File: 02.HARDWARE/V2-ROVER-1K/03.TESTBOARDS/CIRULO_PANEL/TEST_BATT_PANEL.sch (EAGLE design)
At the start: 14 parts, among them J1 302-S201, Q1 PJA3416AE_R1_00001, U3 ATE1D-5M3-10-Z

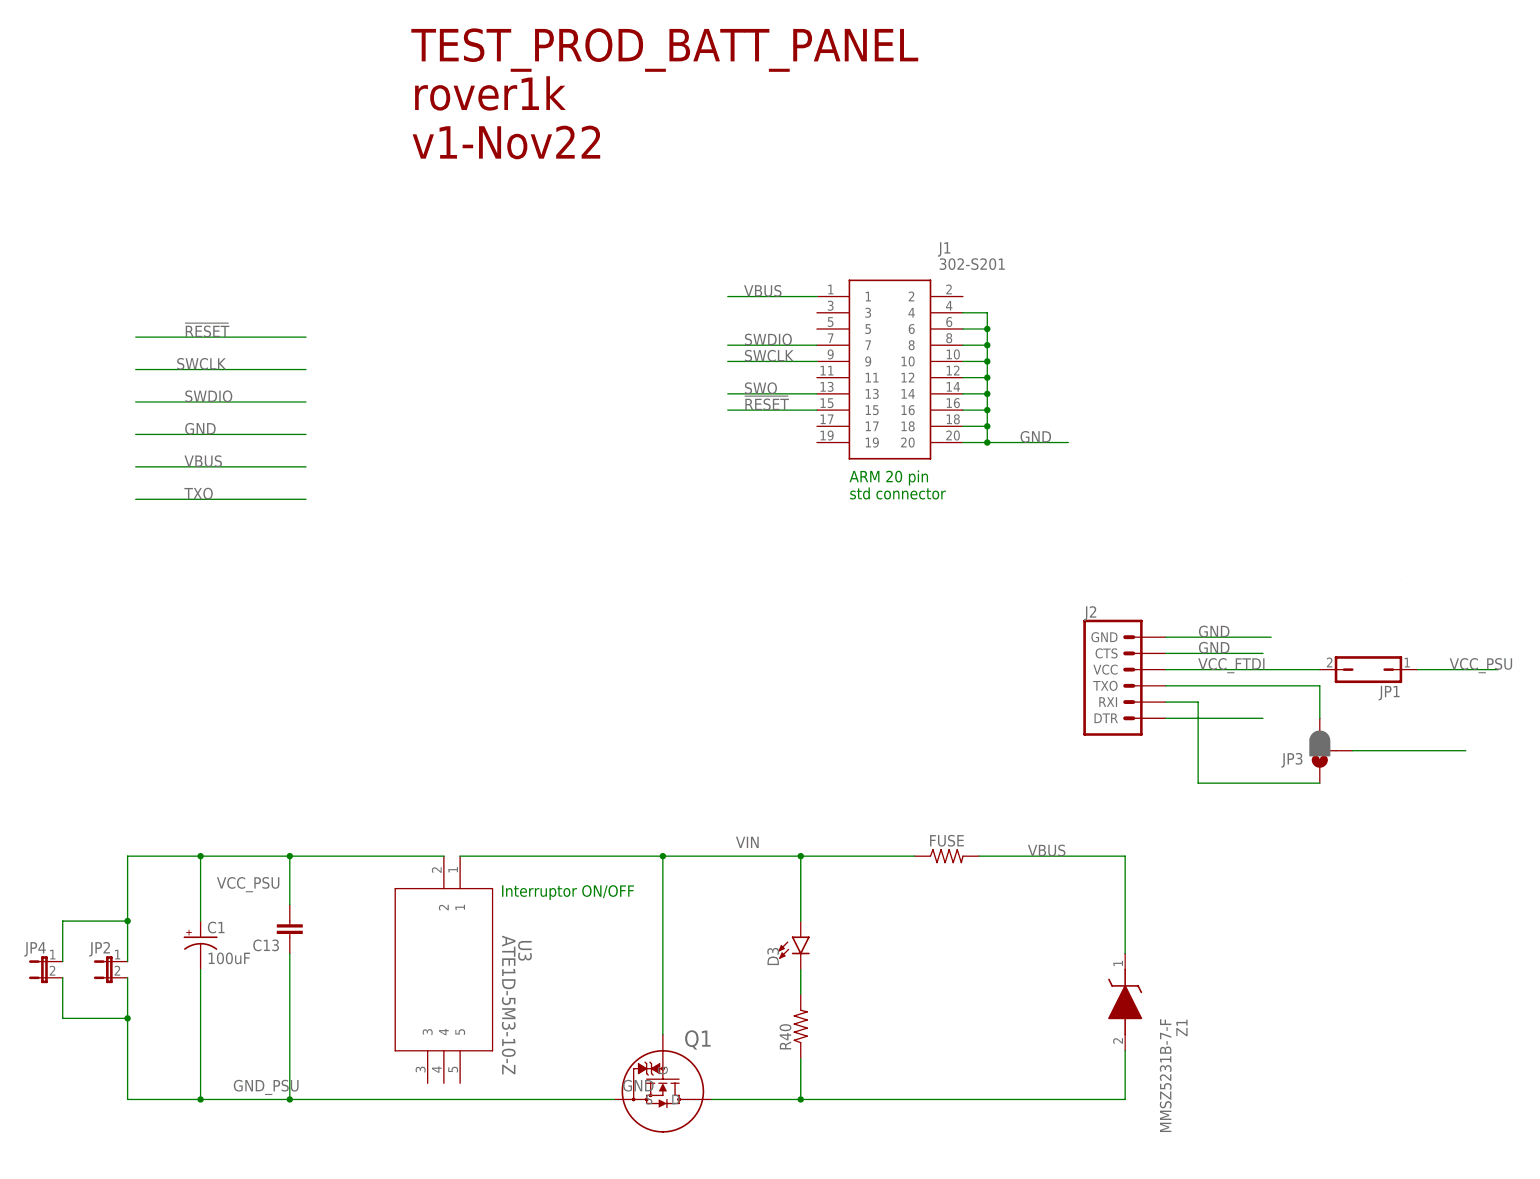
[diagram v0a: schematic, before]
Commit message: Versiones v2 pendientes de revision de conjunto de PCBs Cirulo programacion.
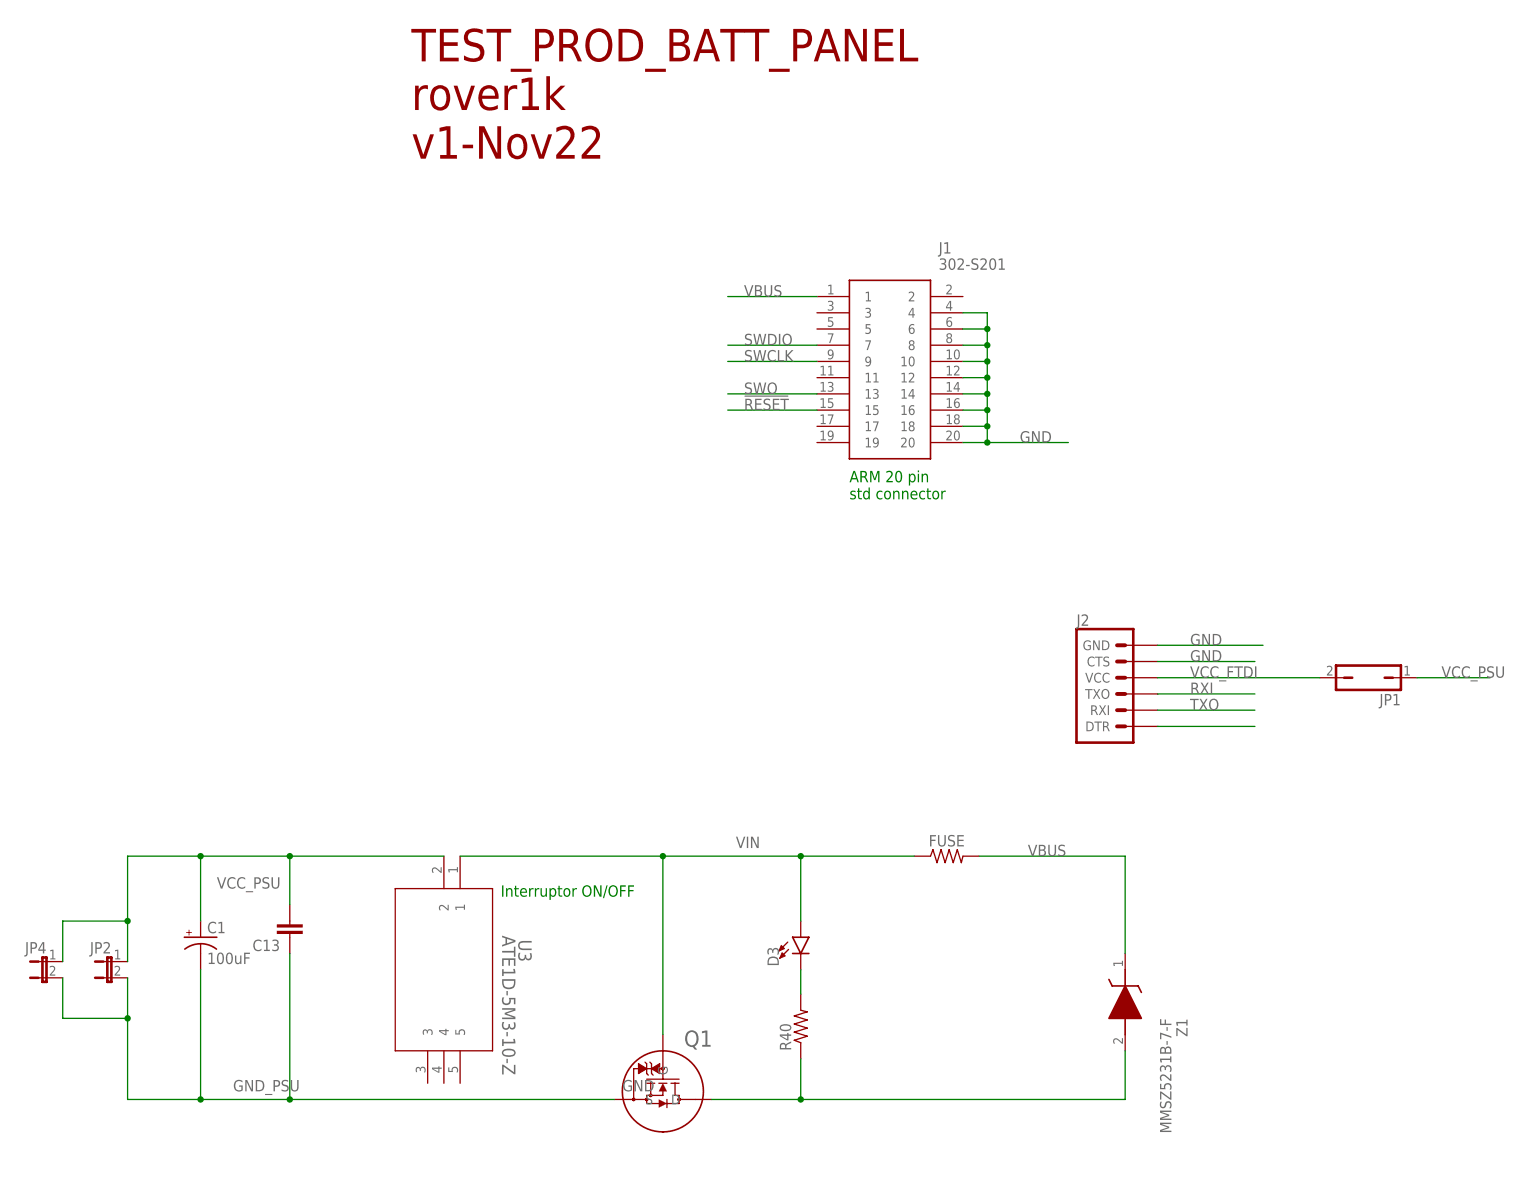
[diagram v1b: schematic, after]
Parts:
- removed JP3: JUMPER-SMT_3_1-NC_PASTE_NO-SILK, SparkFun-Jumpers:JUMPER-SMT_3_1-NC_PASTE_NO-SILK
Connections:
- removed net N$2: J2.RXI, JP3.1
- removed net N$3: J2.TXO, JP3.3
- new net RXI: J2.TXO
- net TXO: now also J2.RXI; no longer JP3.2
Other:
- moved on the sheet: J2, JP1
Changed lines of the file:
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@@
 <drawing>
 <settings>
-<setting alwaysvectorfont="no"/>
+<setting alwaysvectorfont="yes"/>
 <setting keepoldvectorfont="yes"/>
 <setting verticaltext="up"/>
@@
 <part name="JP4" library="jumper" library_urn="urn:adsk.eagle:library:252" deviceset="JP1E" device="" package3d_urn="urn:adsk.eagle:package:15455/1"/>
 <part name="C1" library="SparkFun-Capacitors" library_urn="urn:adsk.eagle:library:510" deviceset="100UF-POLAR" device="-RADIAL-2.5MM-25V-20%" package3d_urn="urn:adsk.eagle:package:37415/1" value="100uF"/>
-<part name="JP3" library="SparkFun-Jumpers" library_urn="urn:adsk.eagle:library:528" deviceset="JUMPER-SMT_3_1-NC_PASTE" device="_NO-SILK" package3d_urn="urn:adsk.eagle:package:39291/1"/>
 </parts>
 <sheets>
@@
 <attribute name="NAME" x="227.1014" y="129.54" size="1.778" layer="95" rot="R90"/>
 </instance>
-<instance part="J2" gate="G$1" x="280.67" y="186.69" smashed="yes">
-<attribute name="VALUE" x="273.05" y="176.784" size="1.778" layer="96" font="vector"/>
-<attribute name="NAME" x="273.05" y="197.358" size="1.778" layer="95" font="vector"/>
+<instance part="J2" gate="G$1" x="279.4" y="185.42" smashed="yes">
+<attribute name="VALUE" x="271.78" y="175.514" size="1.778" layer="96" font="vector"/>
+<attribute name="NAME" x="271.78" y="196.088" size="1.778" layer="95" font="vector"/>
 </instance>
-<instance part="JP1" gate="A" x="317.5" y="189.23" smashed="yes" rot="R90">
-<attribute name="NAME" x="322.58" y="186.69" size="1.778" layer="95" rot="R180"/>
-<attribute name="VALUE" x="322.58" y="193.675" size="1.778" layer="96" rot="R180"/>
+<instance part="JP1" gate="A" x="317.5" y="187.96" smashed="yes" rot="R90">
+<attribute name="NAME" x="322.58" y="185.42" size="1.778" layer="95" rot="R180"/>
+<attribute name="VALUE" x="322.58" y="192.405" size="1.778" layer="96" rot="R180"/>
 </instance>
 <instance part="Z1" gate="G$1" x="279.4" y="144.78" smashed="yes" rot="R270">
@@
 <attribute name="VALUE" x="135.636" y="143.129" size="1.778" layer="96" font="vector"/>
 </instance>
-<instance part="JP3" gate="G$1" x="309.88" y="176.53" smashed="yes" rot="R180">
-<attribute name="NAME" x="307.34" y="176.149" size="1.778" layer="95" font="vector" rot="R180"/>
-</instance>
 </instances>
 <busses>
@@
 <net name="VBUS" class="0">
 <segment>
-<wire x1="124.46" y1="220.98" x2="151.13" y2="220.98" width="0.1524" layer="91"/>
-<label x="132.08" y="220.98" size="1.778" layer="95"/>
-</segment>
-<segment>
 <pinref part="FUSE" gate="G$1" pin="2"/>
 <pinref part="Z1" gate="G$1" pin="K"/>
@@
 <label x="219.71" y="240.03" size="1.778" layer="95"/>
 </segment>
-<segment>
-<wire x1="124.46" y1="231.14" x2="151.13" y2="231.14" width="0.1524" layer="91"/>
-<label x="132.08" y="231.14" size="1.778" layer="95"/>
-</segment>
 </net>
 <net name="SWCLK" class="0">
@@
 <label x="219.71" y="237.49" size="1.778" layer="95"/>
 </segment>
-<segment>
-<wire x1="124.46" y1="236.22" x2="151.13" y2="236.22" width="0.1524" layer="91"/>
-<label x="130.81" y="236.22" size="1.778" layer="95"/>
-</segment>
 </net>
 <net name="SWO" class="0">
@@
 <label x="219.71" y="229.87" size="1.778" layer="95"/>
 </segment>
-<segment>
-<wire x1="124.46" y1="241.3" x2="151.13" y2="241.3" width="0.1524" layer="91"/>
-<label x="132.08" y="241.3" size="1.778" layer="95"/>
-</segment>
 </net>
 <net name="GND" class="0">
@@
 </segment>
 <segment>
-<wire x1="124.46" y1="226.06" x2="151.13" y2="226.06" width="0.1524" layer="91"/>
-<label x="132.08" y="226.06" size="1.778" layer="95"/>
-</segment>
-<segment>
 <pinref part="J2" gate="G$1" pin="GND"/>
-<wire x1="285.75" y1="194.31" x2="302.26" y2="194.31" width="0.1524" layer="91"/>
-<label x="290.83" y="194.31" size="1.778" layer="95"/>
+<wire x1="284.48" y1="193.04" x2="300.99" y2="193.04" width="0.1524" layer="91"/>
+<label x="289.56" y="193.04" size="1.778" layer="95"/>
 </segment>
 <segment>
 <pinref part="J2" gate="G$1" pin="CTS"/>
-<wire x1="285.75" y1="191.77" x2="300.99" y2="191.77" width="0.1524" layer="91"/>
-<label x="290.83" y="191.77" size="1.778" layer="95"/>
+<wire x1="284.48" y1="190.5" x2="299.72" y2="190.5" width="0.1524" layer="91"/>
+<label x="289.56" y="190.5" size="1.778" layer="95"/>
 </segment>
 <segment>
@@
 <segment>
 <pinref part="JP1" gate="A" pin="1"/>
-<wire x1="325.12" y1="189.23" x2="337.82" y2="189.23" width="0.1524" layer="91"/>
-<label x="330.2" y="189.23" size="1.778" layer="95"/>
+<wire x1="325.12" y1="187.96" x2="336.55" y2="187.96" width="0.1524" layer="91"/>
+<label x="328.93" y="187.96" size="1.778" layer="95"/>
 </segment>
 </net>
@@
 <segment>
 <pinref part="J2" gate="G$1" pin="VCC"/>
-<wire x1="285.75" y1="189.23" x2="309.88" y2="189.23" width="0.1524" layer="91"/>
-<label x="290.83" y="189.23" size="1.778" layer="95"/>
+<wire x1="284.48" y1="187.96" x2="309.88" y2="187.96" width="0.1524" layer="91"/>
+<label x="289.56" y="187.96" size="1.778" layer="95"/>
 <pinref part="JP1" gate="A" pin="2"/>
 </segment>
@@
 <net name="TXO" class="0">
 <segment>
-<wire x1="124.46" y1="215.9" x2="151.13" y2="215.9" width="0.1524" layer="91"/>
-<label x="132.08" y="215.9" size="1.778" layer="95"/>
-</segment>
-<segment>
-<pinref part="JP3" gate="G$1" pin="2"/>
-<wire x1="314.96" y1="176.53" x2="332.74" y2="176.53" width="0.1524" layer="91"/>
-<label x="321.31" y="176.53" size="0.0508" layer="95" font="vector"/>
-<label x="322.58" y="203.2" size="0.0508" layer="95" font="vector"/>
-<label x="332.74" y="176.53" size="0.0508" layer="95" font="vector"/>
+<pinref part="J2" gate="G$1" pin="RXI"/>
+<wire x1="284.48" y1="182.88" x2="299.72" y2="182.88" width="0.1524" layer="91"/>
+<label x="289.56" y="182.88" size="1.778" layer="95"/>
 </segment>
 </net>
@@
 <segment>
 <pinref part="J2" gate="G$1" pin="DTR"/>
-<wire x1="285.75" y1="181.61" x2="300.99" y2="181.61" width="0.1524" layer="91"/>
-</segment>
-</net>
-<net name="N$2" class="0">
-<segment>
-<pinref part="J2" gate="G$1" pin="RXI"/>
-<wire x1="285.75" y1="184.15" x2="290.83" y2="184.15" width="0.1524" layer="91"/>
-<wire x1="290.83" y1="184.15" x2="290.83" y2="171.45" width="0.1524" layer="91"/>
-<pinref part="JP3" gate="G$1" pin="1"/>
-<wire x1="290.83" y1="171.45" x2="309.88" y2="171.45" width="0.1524" layer="91"/>
+<wire x1="284.48" y1="180.34" x2="299.72" y2="180.34" width="0.1524" layer="91"/>
 </segment>
 </net>
-<net name="N$3" class="0">
+<net name="RXI" class="0">
 <segment>
 <pinref part="J2" gate="G$1" pin="TXO"/>
-<wire x1="285.75" y1="186.69" x2="309.88" y2="186.69" width="0.1524" layer="91"/>
-<pinref part="JP3" gate="G$1" pin="3"/>
-<wire x1="309.88" y1="186.69" x2="309.88" y2="181.61" width="0.1524" layer="91"/>
+<wire x1="284.48" y1="185.42" x2="299.72" y2="185.42" width="0.1524" layer="91"/>
+<label x="289.56" y="185.42" size="1.778" layer="95"/>
 </segment>
 </net>
